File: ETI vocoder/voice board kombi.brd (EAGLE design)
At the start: 160 x 61 mm, 174 parts, among them IC1 TL072P, IC1. TL072P, IC2 TL072P, IC2. TL072P, IC3 TL081P, IC3. TL081P, IC4 TL081P, IC4. TL081P, IC5 TL072P, IC6 LM13600AN, IC7 TL072P, IC7. TL072P, Q1 BF244C, Q1. BF244C, Q2 BC212L, Q2. BC212L

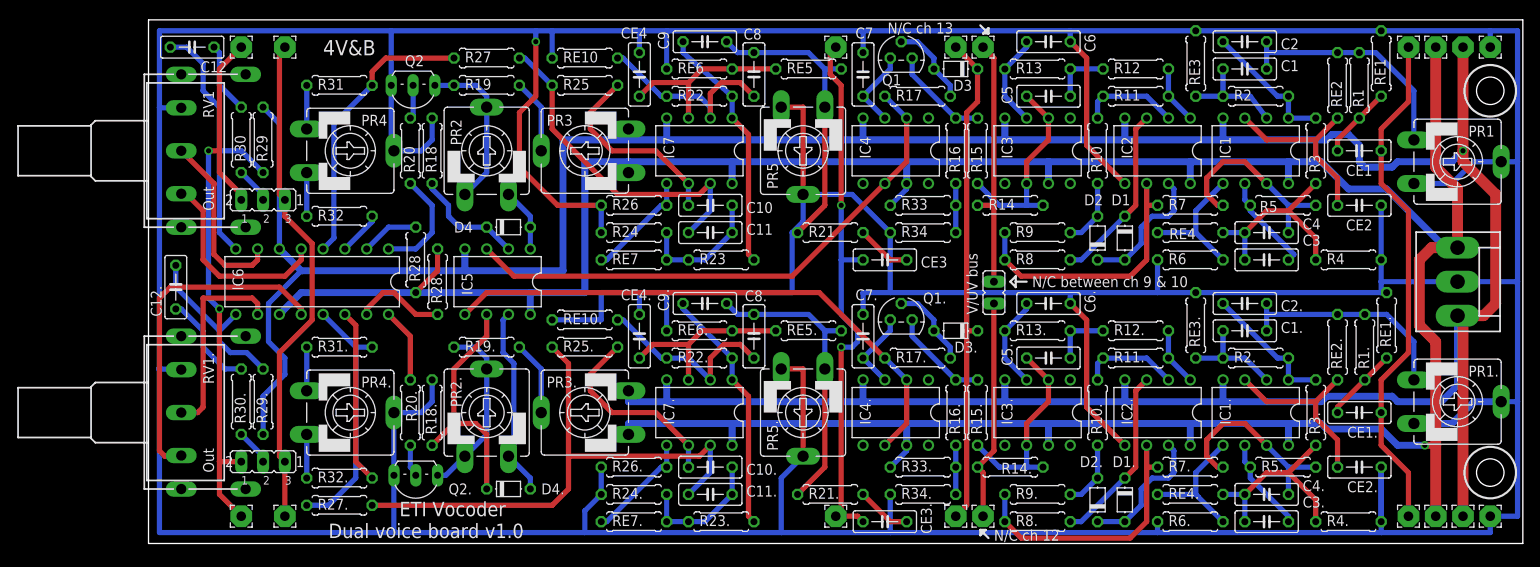
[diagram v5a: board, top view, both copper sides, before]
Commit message: Switched to dual footprint caps for all caps (5mm, 7.5mm). Added footprint to custom library
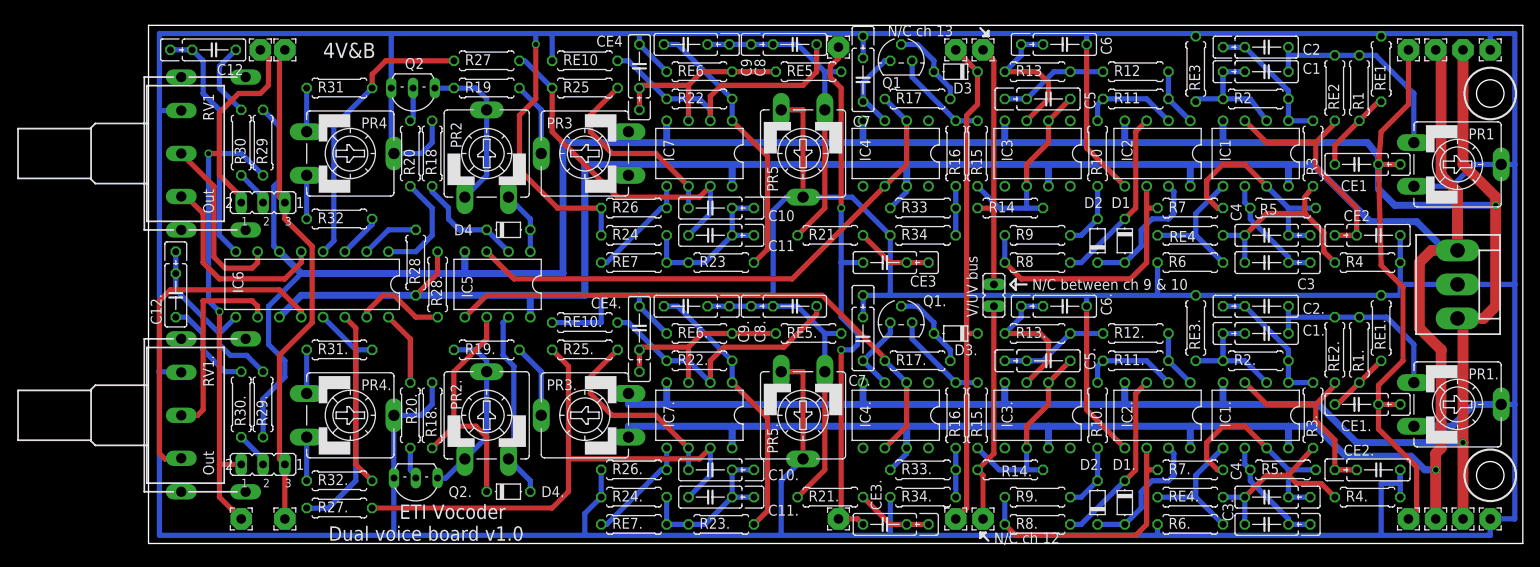
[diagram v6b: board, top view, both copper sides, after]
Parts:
- C1, C1., C10, C10., C11, C11., C12, C12., C2, C2., C3, C3., C4, C4., C5, C5., C6, C6., C7, C7., C8, C8., C9, C9., CE1, CE1., CE2, CE2., CE3, CE3., CE4, CE4.: device resistor:C050-025X075 -> joakim:C050_075-025X100J
- moved C8 5.91 mm to (75.2, 58.1), turned to 180 degrees
- moved C8. 5.91 mm to (75.2, 27.6), turned to 180 degrees
- moved CE2 4.14 mm to (143.2, 35.9)
- moved R4. 3.62 mm to (141.9, 5.40)
- moved C2 2.62 mm to (130.2, 57.8)
- moved C2. 2.56 mm to (130.2, 27.6)
- moved C1. 2.56 mm to (130.2, 24.4)
- moved C1 2.56 mm to (130.2, 54.9)
- moved C12 2.56 mm to (7.62, 57.5)
- moved R4 2.25 mm to (141.9, 32.7)
- moved PAD17 2.25 mm to (13.0, 57.5)
- moved C9 2.25 mm to (62.5, 58.1)
- moved C9. 2.25 mm to (62.5, 27.6)
- moved CE2. 2.25 mm to (143.2, 8.57)
- moved C6 1.93 mm to (106.7, 58.1)
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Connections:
- net GND: now also C7..2, C7..3, C7.2, C7.3; no longer C7..1, C7.1
- net N$1: now also C1.3
- net N$14: now also C5.3
- net N$16: now also C6.3
- net N$18: now also C7.1; no longer C7.2
- net N$27: now also C8.3, C9.3
- net N$28: now also C10.3, C11.3
- net N$3: now also C2.3
- net N$33: now also C12.3
- net N$43: now also CE1.1; no longer CE1.2
- net N$44: now also CE2.3
- net N$45: now also CE3.3
- net N$46: now also CE4.3
- net N$47: now also C1..3
- net N$49: now also C2..3
- net N$51: now also C3..3
- net N$53: now also C4..3
- net N$6: now also C3.3
- net N$60: now also C5..3
- net N$62: now also C6..3
- net N$64: now also C7..1; no longer C7..2
- net N$73: now also C8..3, C9..3
- net N$74: now also C10..3, C11..3
- net N$8: now also C4.3
- net N$84: now also C12..3
- net N$88: now also CE1..1; no longer CE1..2
- net N$89: now also CE2..3
- net N$90: now also CE3..3
- net N$91: now also CE4..3
- net SPEECH_IN: now also CE1..2, CE1..3, CE1.2, CE1.3; no longer CE1..1, CE1.1
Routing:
- net N$29: track 23.6 -> 34.0 mm
- net GND: track 823.9 -> 814.3 mm
- net N$75: track 22.6 -> 31.8 mm
- net N$62: track 11.0 -> 17.8 mm
- net N$16: track 11.0 -> 17.6 mm
- net N$44: track 21.6 -> 28.1 mm
- net N$14: track 6.98 -> 12.7 mm
- net N$60: track 6.99 -> 12.7 mm
- net SPEECH_IN: track 59.9 -> 65.5 mm
- net N$28: track 15.3 -> 20.4 mm
- net N$74: track 15.3 -> 20.4 mm
- net +12V: track 356.0 -> 359.4 mm
- net OUT2: track 67.8 -> 71.0 mm
- net N$76: track 28.8 -> 32.0 mm
- net N$30: track 29.0 -> 32.0 mm
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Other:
- board size 160 x 61 mm -> 160 x 60.3 mm

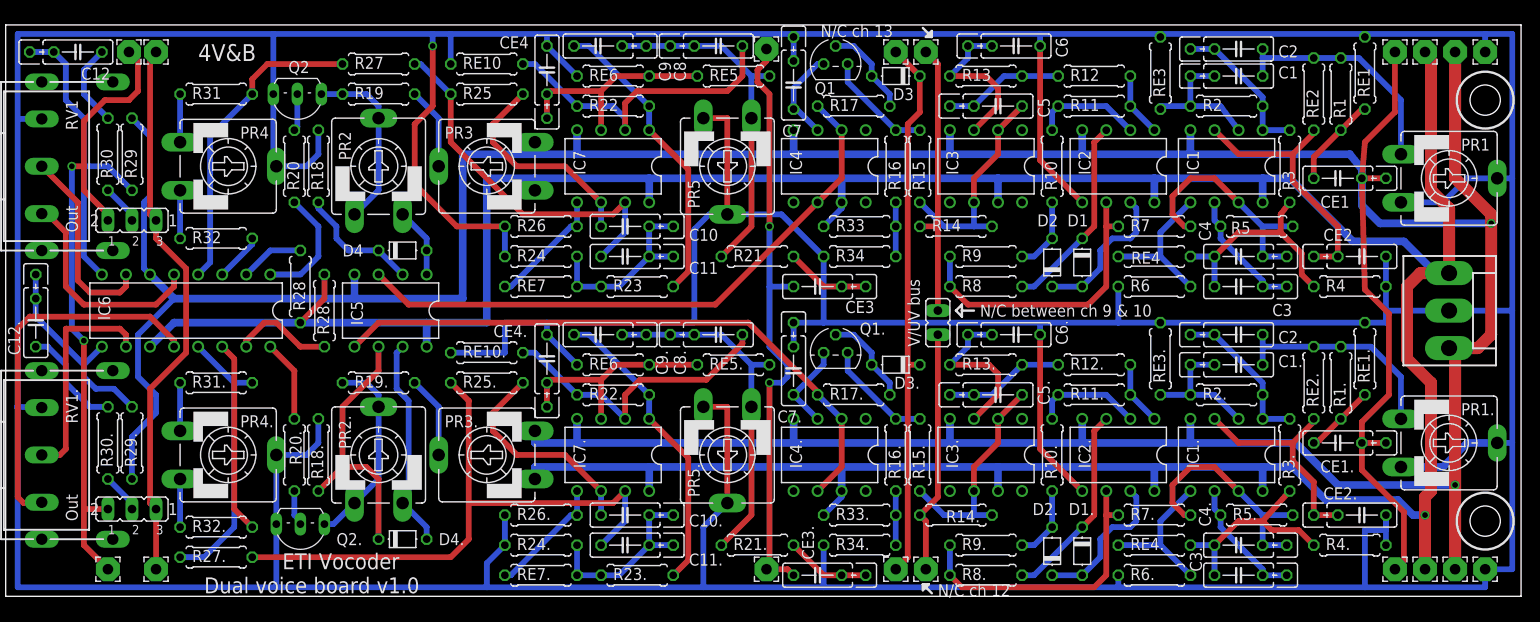
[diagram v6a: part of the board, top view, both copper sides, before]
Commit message: Replaced all c/r combinations with special component
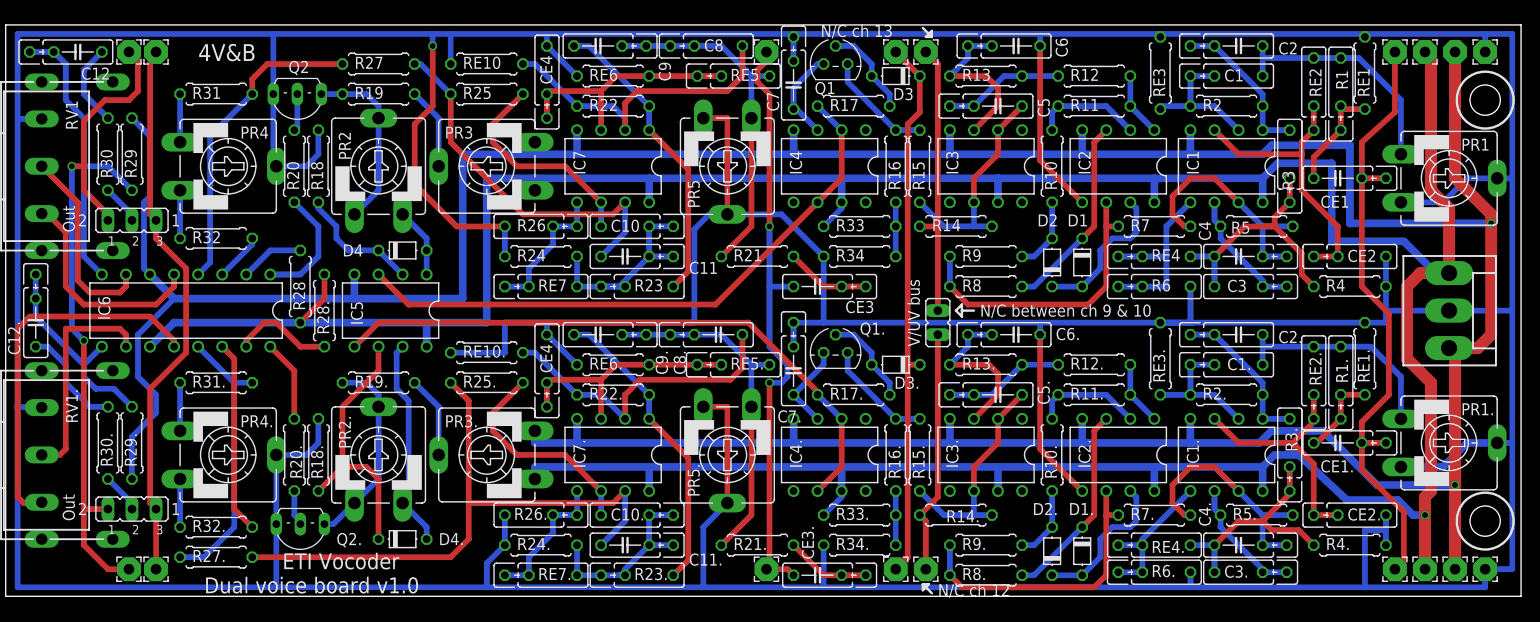
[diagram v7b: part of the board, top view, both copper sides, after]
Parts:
- C1, C1., C10, C10., C3, C3., C8, CE2, CE2., CE4, CE4.: value (none) -> C-OR-R050_075-025X100; device joakim:C050_075-025X100J -> joakim:P050_075-025X100J
- R1, R1., R23, R23., R26, R26., R3, R3., R6, R6., RE2, RE2., RE4, RE4., RE5, RE5., RE7, RE7.: value (none) -> C-OR-R050_075-025X100; device resistor:0207/7 -> joakim:P050_075-025X100J
- moved PAD18 2.22 mm to (13.0, 2.86)
- moved C3. 1.31 mm to (131.4, 2.54)
- moved C1 1.27 mm to (128.9, 54.9)
- moved C1. 1.27 mm to (128.9, 24.4)
- moved CE4 1.27 mm to (57.1, 54.3)
- moved CE4. 1.27 mm to (57.1, 23.8)
- moved C10 1.27 mm to (66.7, 39.1)
- moved C10. 1.27 mm to (66.7, 8.57)
- moved C8 1.27 mm to (74.0, 58.1)
- moved C3 1.27 mm to (131.4, 32.7)
- moved CE2 1.27 mm to (141.9, 35.9)
- moved CE2. 1.27 mm to (141.9, 8.57)
- moved C2 0.32 mm to (130.2, 58.1)
- moved R6. 0.32 mm to (121.3, 2.54), turned to 180 degrees
- moved PAD3 0.32 mm to (80.3, 57.5)
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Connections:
- net N$2: now also R1.1; no longer R1.2
- net N$28: now also R23.3
- net N$32: now also R26.3, RE7.3
- net N$43: now also R1.2, R1.3; no longer R1.1
- net N$44: now also RE2.3
- net N$46: now also RE5.3
- net N$48: now also R1..1; no longer R1..2
- net N$5: now also R3.3
- net N$50: now also R3..3
- net N$52: now also R6..3, RE4..3
- net N$7: now also R6.3, RE4.3
- net N$74: now also R23..3
- net N$87: now also R26..3, RE7..3
- net N$88: now also R1..2, R1..3; no longer R1..1
- net N$89: now also RE2..3
- net N$91: now also RE5..3
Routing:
- net +12V: track 359.4 -> 366.6 mm
- net -12V: track 393.7 -> 398.0 mm
- net N$7: track 16.0 -> 20.1 mm
- net N$87: track 12.8 -> 16.9 mm
- net GND: track 814.3 -> 817.8 mm
- net N$28: track 20.4 -> 23.5 mm
- net N$5: track 24.4 -> 27.2 mm
- net N$44: track 28.1 -> 30.8 mm
- net N$89: track 23.8 -> 26.4 mm
- net N$91: track 23.3 -> 25.9 mm
- net N$46: track 23.3 -> 25.9 mm
- net N$50: track 22.6 -> 24.9 mm
- net N$32: track 12.8 -> 15.0 mm
- net OUT2: track 71.0 -> 73.2 mm
- net N$43: track 9.72 -> 11.7 mm
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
